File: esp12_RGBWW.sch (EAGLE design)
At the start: 38 parts, among them Q1 AOD2910SMD, Q2 AOD2910SMD, Q3 AOD2910SMD, Q4 AOD2910SMD, Q5 AOD2910SMD, U1 TPS5410DR

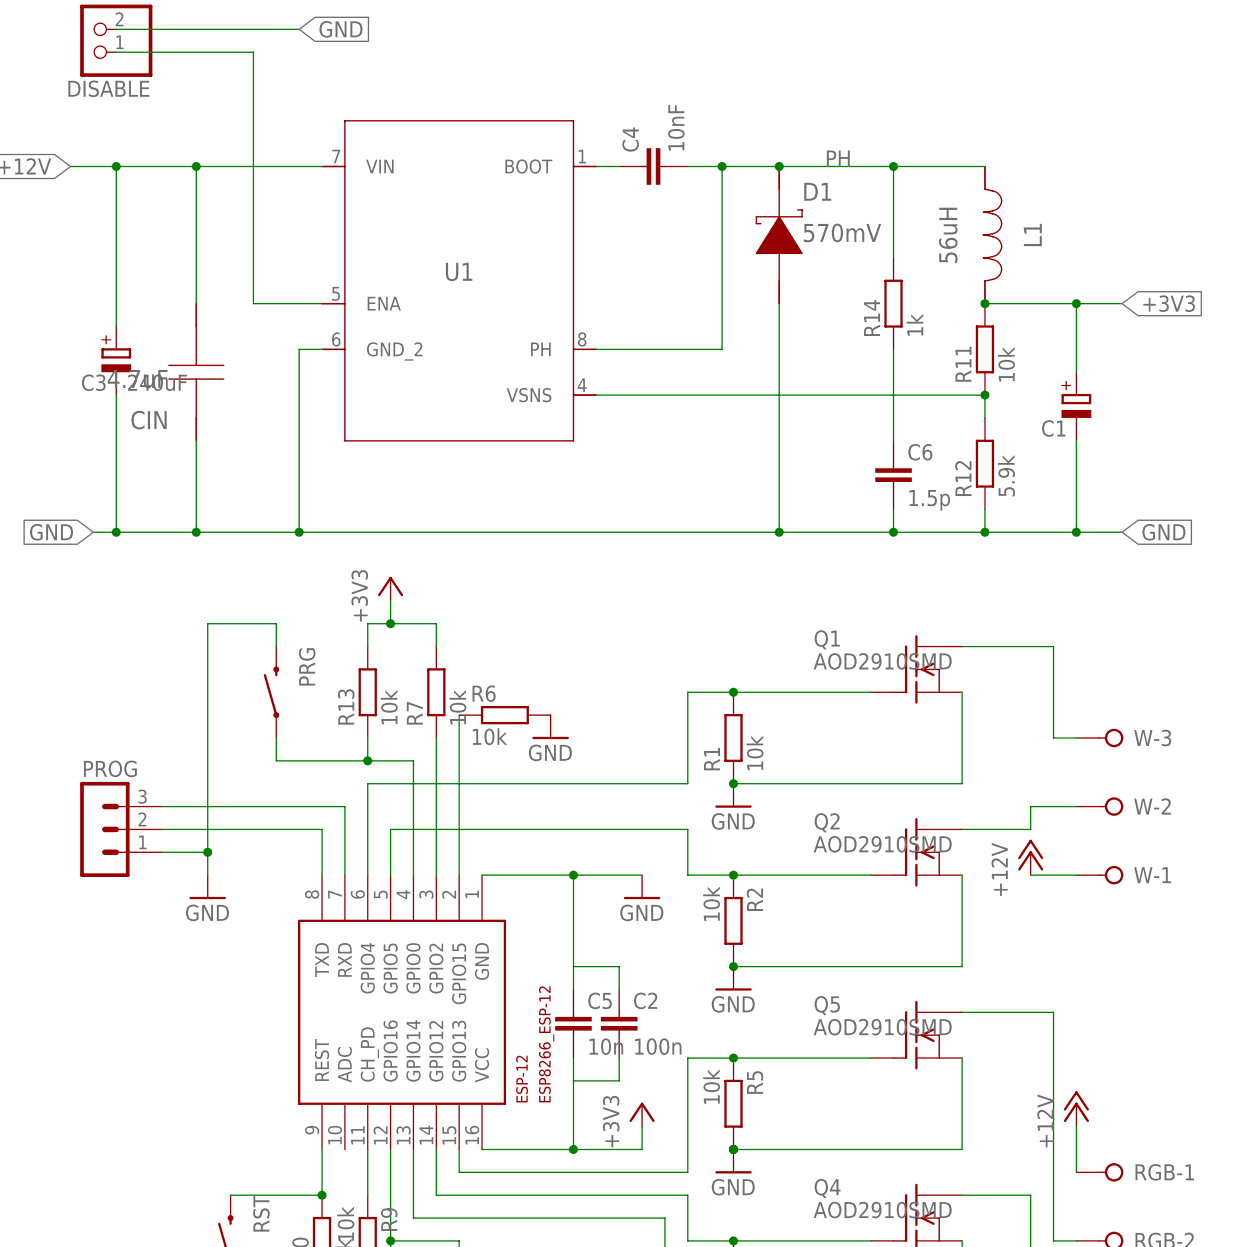
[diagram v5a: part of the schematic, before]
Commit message: yet more minor changes on the input side
removed the snubber pads
created a lower impedance GND path
swiched RXD and TXD for some more elegant routing and better fit with the usual USB/UART connectors (straight cable now switches RX/TX)
minor silkscreen corrections for better legibility
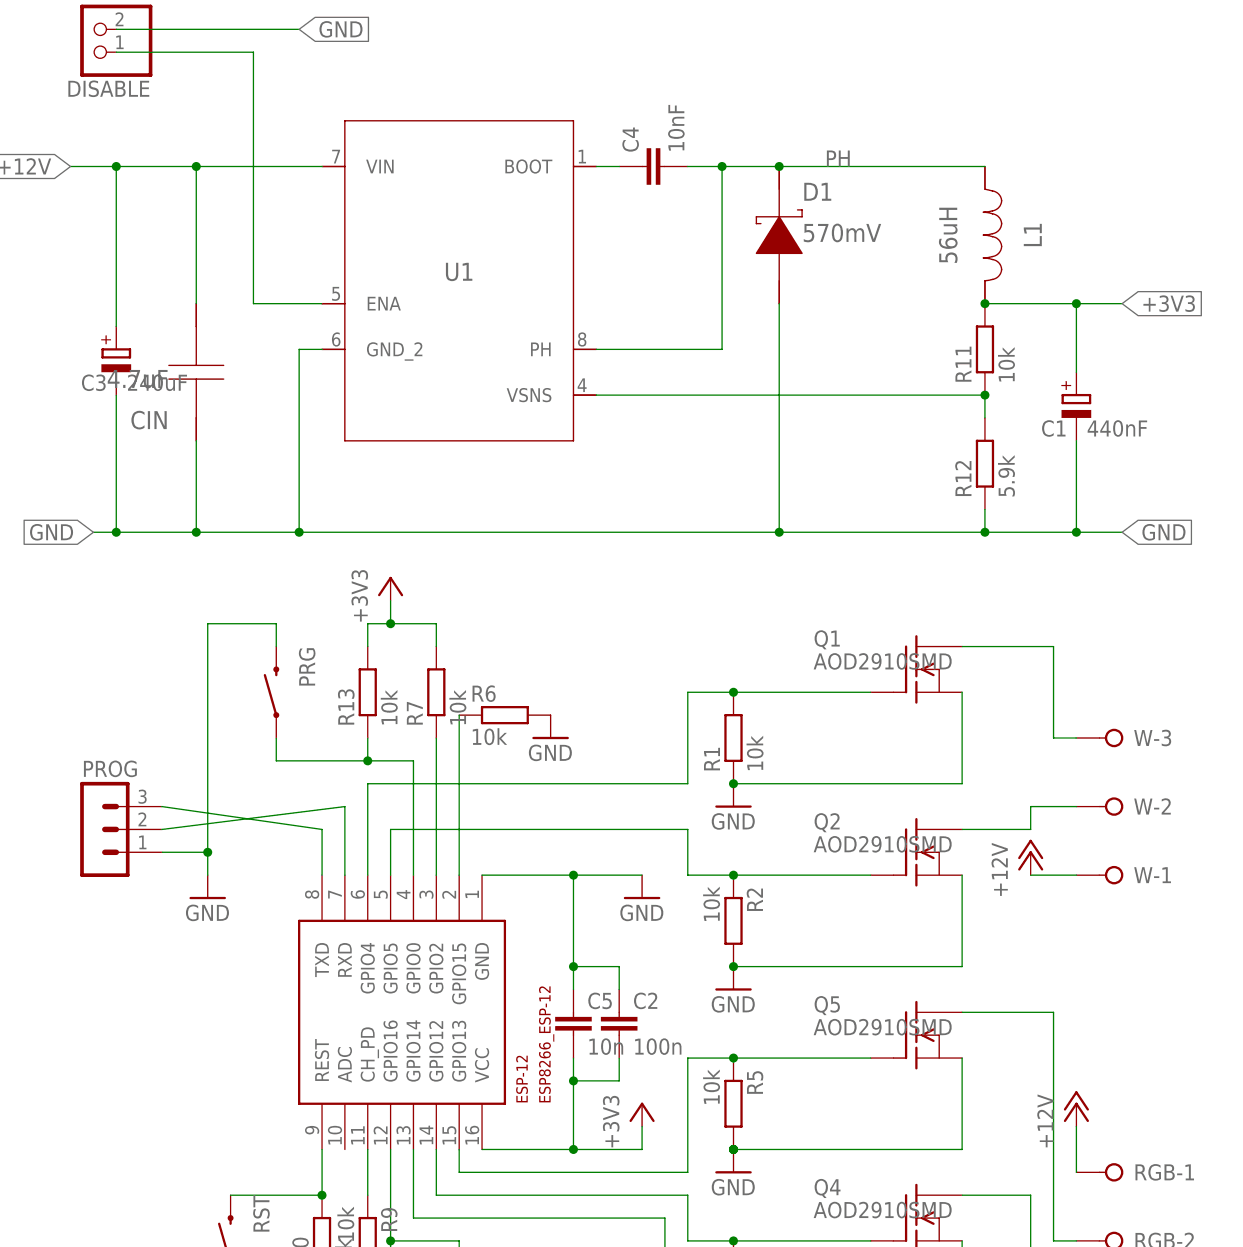
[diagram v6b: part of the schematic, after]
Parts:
- removed C6: 1.5p, rcl:C-EUC0805
- removed R14: 1k, rcl:R-EU_R0805
- C1: value (none) -> 440nF
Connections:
- removed net SNUB: C6.1, R14.1
- net GND: no longer C6.2
- net PH: no longer R14.2
- net RXD: now also PROG.2; no longer PROG.3
- net TXD: now also PROG.3; no longer PROG.2
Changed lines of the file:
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@@
 <part name="R8" library="rcl" deviceset="R-EU_" device="R0805" value="10k"/>
 <part name="GND14" library="supply1" deviceset="GND" device=""/>
-<part name="C1" library="resistor" deviceset="CPOL-EU" device="E2.5-7"/>
+<part name="C1" library="resistor" deviceset="CPOL-EU" device="E2.5-7" value="440nF"/>
 <part name="CIN" library="AcceleratedDesigns_Lib" deviceset="GRM31CR71H475KA12L" device="" value="4.7uF"/>
 <part name="D1" library="TI_Accelerated_Design_neu" deviceset="B160-13-F" device="" value="570mV"/>
@@
 <part name="C3" library="resistor" deviceset="CPOL-EU" device="E2.5-7" value="240uF"/>
 <part name="PROG" library="con-lstb" deviceset="MA03-1" device=""/>
-<part name="R14" library="rcl" deviceset="R-EU_" device="R0805" value="1k"/>
 <part name="C5" library="rcl" deviceset="C-EU" device="C0805" value="10n"/>
-<part name="C6" library="rcl" deviceset="C-EU" device="C0805" value="1.5p"/>
 <part name="DISABLE" library="pinhead" deviceset="PINHD-1X2" device=""/>
 </parts>
@@
 </instance>
 <instance part="PROG" gate="G$1" x="2.54" y="50.8"/>
-<instance part="R14" gate="G$1" x="91.44" y="109.22" rot="R90"/>
 <instance part="C5" gate="G$1" x="55.88" y="30.48"/>
-<instance part="C6" gate="G$1" x="91.44" y="91.44"/>
 <instance part="DISABLE" gate="G$1" x="2.54" y="139.7" rot="R180"/>
 </instances>
@@
 <pinref part="C5" gate="G$1" pin="1"/>
 <wire x1="55.88" y1="33.02" x2="55.88" y2="35.56" width="0.1524" layer="91"/>
+<junction x="55.88" y="35.56"/>
 </segment>
 <segment>
@@
 <wire x1="13.97" y1="83.82" x2="25.4" y2="83.82" width="0.1524" layer="91"/>
 <wire x1="25.4" y1="83.82" x2="78.74" y2="83.82" width="0.1524" layer="91"/>
-<wire x1="78.74" y1="83.82" x2="91.44" y2="83.82" width="0.1524" layer="91"/>
-<wire x1="91.44" y1="83.82" x2="101.6" y2="83.82" width="0.1524" layer="91"/>
+<wire x1="78.74" y1="83.82" x2="101.6" y2="83.82" width="0.1524" layer="91"/>
 <wire x1="101.6" y1="83.82" x2="111.76" y2="83.82" width="0.1524" layer="91"/>
 <pinref part="U1" gate="A" pin="GND_2"/>
@@
 <wire x1="111.76" y1="93.98" x2="111.76" y2="83.82" width="0.1524" layer="91"/>
 <junction x="111.76" y="83.82"/>
-<pinref part="C6" gate="G$1" pin="2"/>
-<wire x1="91.44" y1="86.36" x2="91.44" y2="83.82" width="0.1524" layer="91"/>
-<junction x="91.44" y="83.82"/>
 <label x="25.4" y="139.7" size="1.778" layer="95" xref="yes"/>
 </segment>
@@
 <pinref part="ESP-12" gate="G$1" pin="RXD"/>
 <wire x1="30.48" y1="53.34" x2="30.48" y2="45.72" width="0.1524" layer="91"/>
+<pinref part="PROG" gate="G$1" pin="2"/>
+<wire x1="10.16" y1="50.8" x2="30.48" y2="53.34" width="0.1524" layer="91"/>
+</segment>
+</net>
+<net name="TXD" class="0">
+<segment>
+<pinref part="ESP-12" gate="G$1" pin="TXD"/>
 <pinref part="PROG" gate="G$1" pin="3"/>
-<wire x1="10.16" y1="53.34" x2="30.48" y2="53.34" width="0.1524" layer="91"/>
-</segment>
-</net>
-<net name="TXD" class="0">
-<segment>
-<pinref part="ESP-12" gate="G$1" pin="TXD"/>
-<pinref part="PROG" gate="G$1" pin="2"/>
-<wire x1="10.16" y1="50.8" x2="27.94" y2="50.8" width="0.1524" layer="91"/>
+<wire x1="10.16" y1="53.34" x2="27.94" y2="50.8" width="0.1524" layer="91"/>
 <wire x1="27.94" y1="50.8" x2="27.94" y2="45.72" width="0.1524" layer="91"/>
 </segment>
@@
 <pinref part="C5" gate="G$1" pin="2"/>
 <wire x1="55.88" y1="22.86" x2="55.88" y2="25.4" width="0.1524" layer="91"/>
+<junction x="55.88" y="22.86"/>
 </segment>
 <segment>
@@
 <pinref part="L1" gate="A" pin="2"/>
 <wire x1="72.39" y1="124.46" x2="78.74" y2="124.46" width="0.1524" layer="91"/>
-<wire x1="78.74" y1="124.46" x2="91.44" y2="124.46" width="0.1524" layer="91"/>
+<wire x1="78.74" y1="124.46" x2="101.6" y2="124.46" width="0.1524" layer="91"/>
 <pinref part="U1" gate="A" pin="PH"/>
-<wire x1="91.44" y1="124.46" x2="101.6" y2="124.46" width="0.1524" layer="91"/>
 <wire x1="58.42" y1="104.14" x2="72.39" y2="104.14" width="0.1524" layer="91"/>
 <wire x1="72.39" y1="104.14" x2="72.39" y2="124.46" width="0.1524" layer="91"/>
@@
 <junction x="72.39" y="124.46"/>
 <label x="83.82" y="124.46" size="1.778" layer="95"/>
-<pinref part="R14" gate="G$1" pin="2"/>
-<wire x1="91.44" y1="114.3" x2="91.44" y2="124.46" width="0.1524" layer="91"/>
-<junction x="91.44" y="124.46"/>
 </segment>
 </net>
@@
 </segment>
 </net>
-<net name="SNUB" class="0">
-<segment>
-<pinref part="R14" gate="G$1" pin="1"/>
-<pinref part="C6" gate="G$1" pin="1"/>
-<wire x1="91.44" y1="104.14" x2="91.44" y2="93.98" width="0.1524" layer="91"/>
-</segment>
-</net>
